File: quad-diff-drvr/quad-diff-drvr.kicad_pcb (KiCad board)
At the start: 2 copper layers, 65 x 56 mm, 58 parts, among them J1 Raspberry_Pi_2_3, J2 Conn_01x04, J3 Conn_01x04, J4 Conn_01x04, J5 Conn_01x04, J6 Conn_01x04, U1 INA3221, U2 74LS153, U3 74LS153, U4 74LS153, U5 PCA9555PW, U6 LTC1688, U7 SLG5NT1581V, U8 SLG5NT1581V

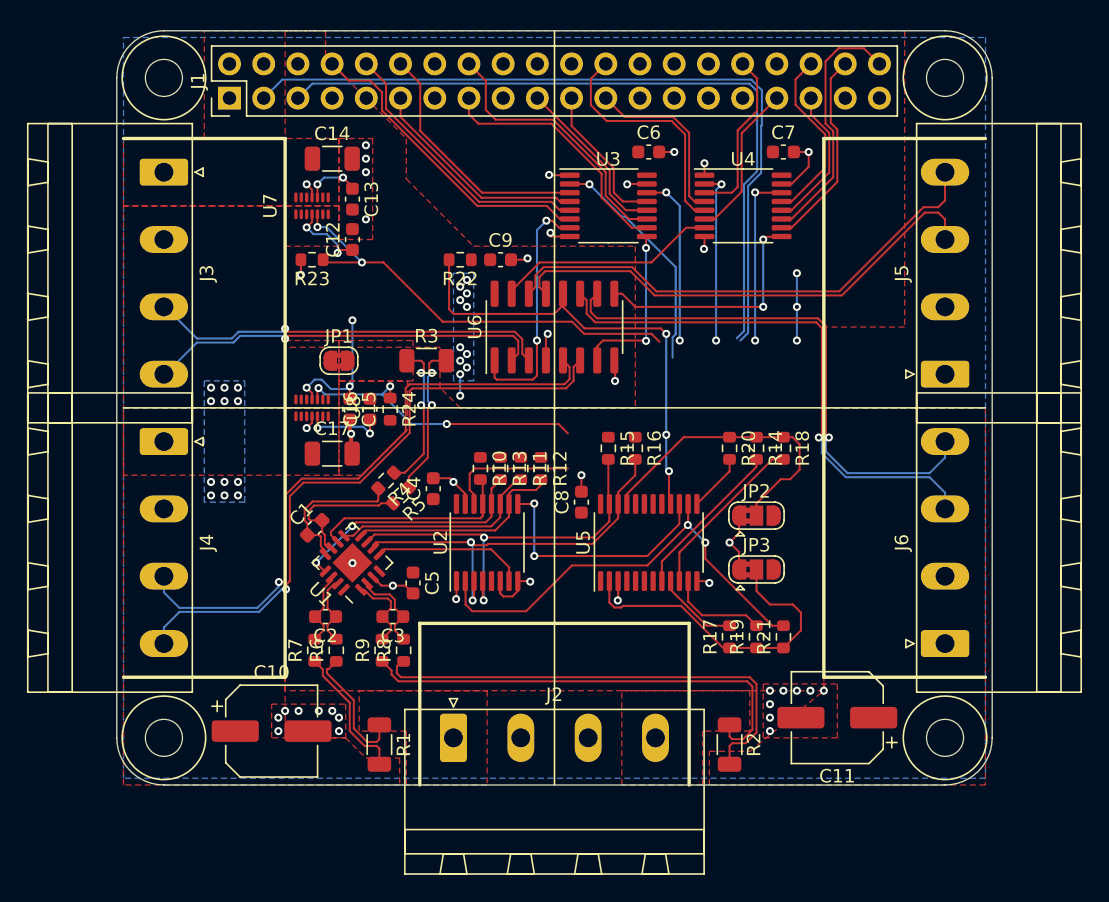
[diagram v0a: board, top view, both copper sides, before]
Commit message: qdd: VB high side switches
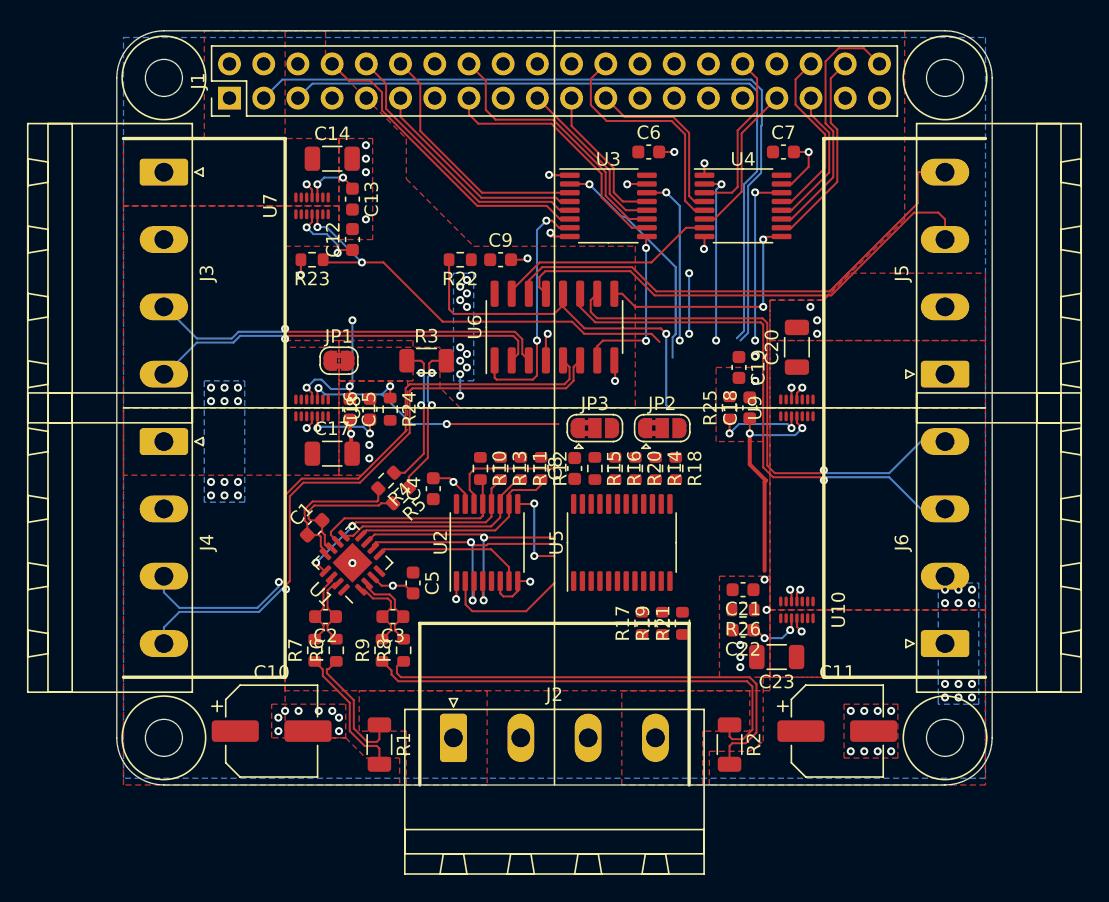
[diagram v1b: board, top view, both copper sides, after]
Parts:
- added C18: 100nF, Capacitor_SMD:C_0603_1608Metric, F.Cu at (114.5, 100.0)
- added C19: 4.7nF, Capacitor_SMD:C_0603_1608Metric, F.Cu at (113.7, 97.0)
- added C20: 10uF, Capacitor_SMD:C_1206_3216Metric, F.Cu at (118.0, 95.5)
- added C21: 100nF, Capacitor_SMD:C_0603_1608Metric, F.Cu at (114.0, 113.5)
- added C22: 4.7nF, Capacitor_SMD:C_0603_1608Metric, F.Cu at (114.0, 116.5)
- added C23: 10uF, Capacitor_SMD:C_1206_3216Metric, F.Cu at (116.5, 118.5)
- added R25: 10k, Resistor_SMD:R_0603_1608Metric, F.Cu at (113.0, 100.0)
- added R26: 10k, Resistor_SMD:R_0603_1608Metric, F.Cu at (114.0, 115.0)
- added U10: SLG5NT1581V, octo-pcb:QFN-28_1x3_Pitch0.4mm, F.Cu at (118.0, 115.0)
- added U9: SLG5NT1581V, octo-pcb:QFN-28_1x3_Pitch0.4mm, F.Cu at (118.0, 100.0)
- moved JP3 15.9 mm to (103.0, 101.5)
- moved JP2 9.55 mm to (108.0, 101.5)
- moved R18 8.14 mm to (109.0, 104.5)
- moved R14 7.65 mm to (107.5, 104.5)
- moved R21 7.57 mm to (109.5, 116.0)
- moved R20 7.16 mm to (106.0, 104.5)
- moved R19 7.07 mm to (108.0, 116.0)
- moved R17 6.58 mm to (106.5, 116.0)
- moved C8 2.55 mm to (101.5, 104.5)
- moved R16 2.12 mm to (104.5, 104.5)
- moved U5 2.00 mm to (105.0, 110.0)
- moved R15 1.80 mm to (103.0, 104.5)
- moved C11 1.00 mm to (121.0, 124.0), turned to 0 degrees
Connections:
- J5 pad 1: /VB -> /VB2
- J6 pad 1: /VB -> /VB3
- U5 pad 6: (no net) -> /VEN2
- U5 pad 7: (no net) -> /VEN3
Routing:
- net /A1: track 24.3 -> 0.00 mm
- net /PM_A1: track 33.6 -> 9.42 mm, vias 2 -> 0
- net /A0: track 22.6 -> 0.00 mm
- net +5V: track 29.8 -> 47.9 mm, vias 18 -> 21
- net /M1_A0: track 25.7 -> 13.0 mm
- net /M0_A0: track 24.8 -> 12.9 mm
- net /PM_STAT: track 18.4 -> 6.64 mm
- net /SCL: track 83.9 -> 73.6 mm
- net /SDA: track 86.7 -> 77.5 mm
- net /M1_A1: track 20.4 -> 13.0 mm
- net /DEN: track 35.6 -> 28.4 mm, vias 3 -> 1
- net /VEN2: track 0.00 -> 6.96 mm, vias 0 -> 2
- net /M0_A1: track 23.4 -> 17.2 mm
- net GND: track 44.1 -> 38.0 mm, vias 43 -> 63
- net /PM_A0: track 14.2 -> 8.84 mm
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- added copper zone on B.Cu, net /VB
- added copper zone on F.Cu, net /VB2
- added copper zone on F.Cu, net /VB3

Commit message: qdd: quick and dirty route done
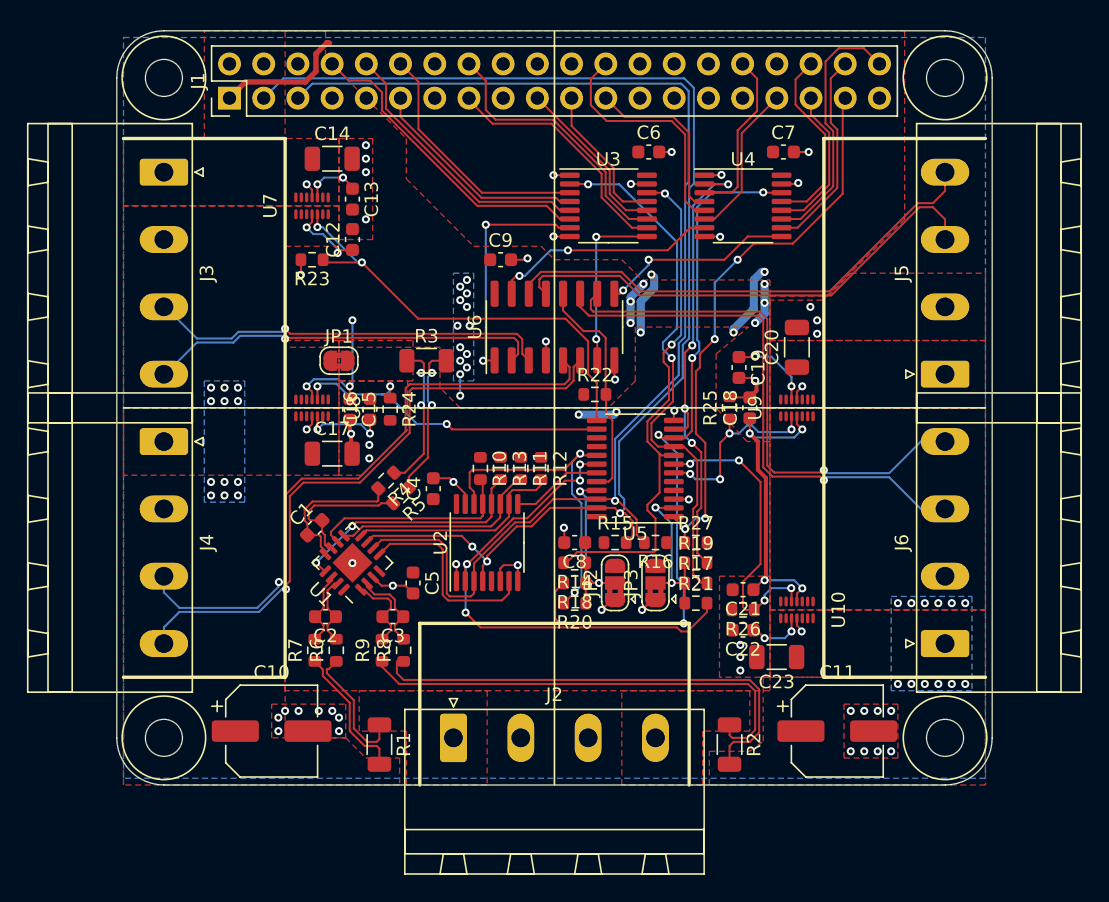
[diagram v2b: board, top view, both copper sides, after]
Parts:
- added R27: 10k, Resistor_SMD:R_0603_1608Metric, F.Cu at (110.5, 110.0)
- moved R22 14.1 mm to (103.0, 99.0), turned to 0 degrees
- moved JP3 12.3 mm to (107.5, 113.0), turned to 90 degrees
- moved JP2 12.0 mm to (104.5, 113.0), turned to 90 degrees
- moved R18 11.3 mm to (101.5, 113.0), turned to 180 degrees
- moved R20 11.0 mm to (101.5, 114.5), turned to 180 degrees
- moved R14 9.22 mm to (101.5, 111.5), turned to 180 degrees
- moved R16 6.26 mm to (107.5, 110.0), turned to 180 degrees
- moved R15 5.70 mm to (104.5, 110.0), turned to 0 degrees
- moved U5 5.59 mm to (106.0, 104.5), turned to 180 degrees
- moved C8 5.50 mm to (101.5, 110.0), turned to 180 degrees
- moved R19 5.15 mm to (110.5, 111.5), turned to 0 degrees
- moved R17 5.00 mm to (110.5, 113.0), turned to 0 degrees
- moved R21 1.80 mm to (110.5, 114.5), turned to 0 degrees
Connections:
- J1 pad 37: (no net) -> /INTn
- U5 pad 1: (no net) -> /INTn
- U5 pad 13: /PM_A0 -> /VEN0
- U5 pad 14: /PM_A1 -> /VEN1
- U5 pad 15: /PM_STAT -> (no net)
- U5 pad 16: /DEN -> (no net)
- U5 pad 17: (no net) -> /PM_A0
- U5 pad 18: (no net) -> /PM_A1
- U5 pad 19: (no net) -> /PM_STAT
- U5 pad 20: (no net) -> /DEN
- U5 pad 4: /VEN0 -> (no net)
- U5 pad 5: /VEN1 -> (no net)
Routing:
- net /INTn: track 0.00 -> 41.9 mm, vias 0 -> 4
- net /M1_A0: track 13.0 -> 53.8 mm, vias 2 -> 4
- net /PM_A1: track 9.42 -> 38.1 mm, vias 0 -> 4
- net /M0_A0: track 12.9 -> 39.2 mm
- net /M0_A1: track 17.2 -> 39.8 mm, vias 1 -> 2
- net /M1_A1: track 13.0 -> 35.3 mm, vias 2 -> 4
- net /VEN3: track 0.92 -> 22.6 mm, vias 3 -> 4
- net /SCL: track 73.6 -> 92.8 mm, vias 2 -> 1
- net +3V3: track 4.50 -> 23.1 mm, vias 2 -> 6
- net /SDA: track 77.5 -> 94.1 mm, vias 2 -> 3
- net /PM_A0: track 8.84 -> 24.7 mm, vias 0 -> 2
- net /A0: track 0.00 -> 14.1 mm, vias 0 -> 2
- net /A1: track 0.00 -> 13.0 mm, vias 0 -> 2
- net +5V: track 47.9 -> 59.3 mm, vias 21 -> 30
- net /DEN: track 28.4 -> 17.3 mm, vias 1 -> 0
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
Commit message: qdd: cleaned up silkscreen
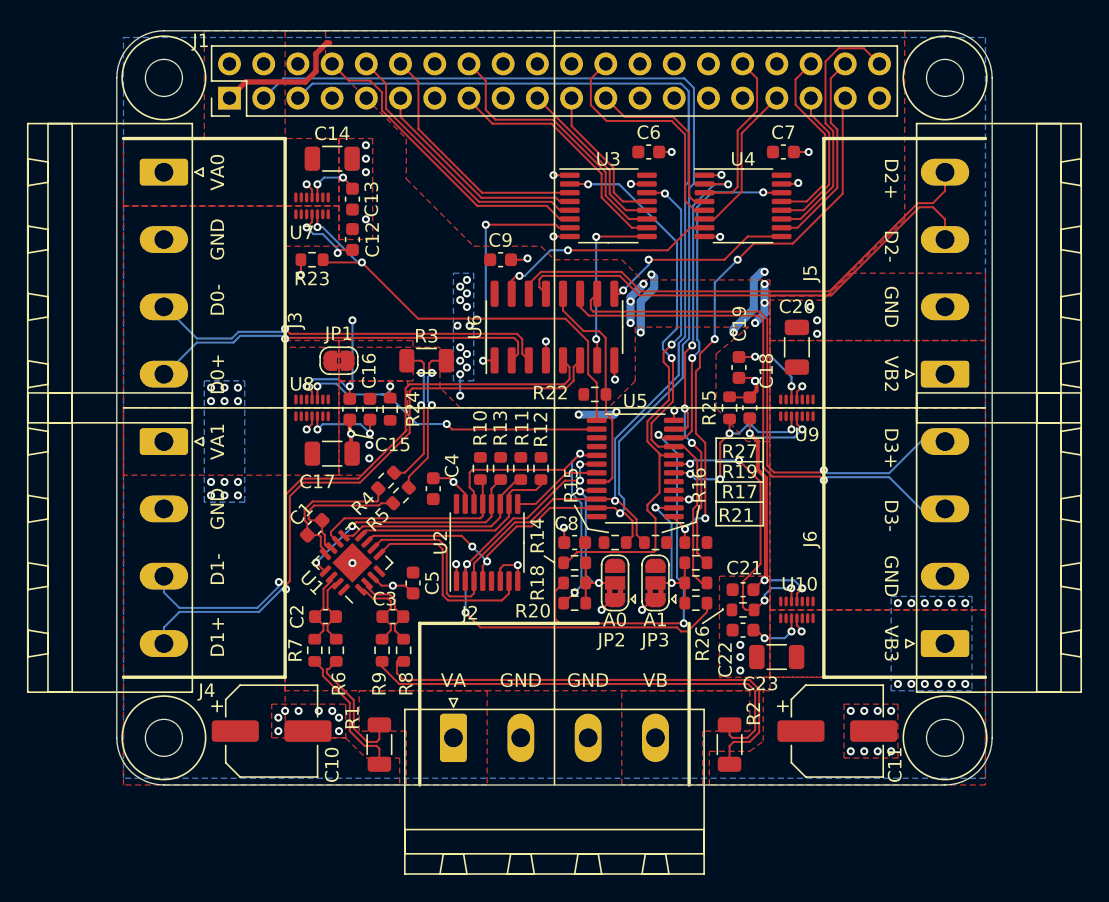
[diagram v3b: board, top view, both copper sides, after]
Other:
- board text added: "A0"
- board text added: "A1"
- board text added: "D0+"
- board text added: "D0-"
- board text added: "D1+"
- board text added: "D1-"
- board text added: "D2+"
- board text added: "D2-"
- board text added: "D3+"
- board text added: "D3-"
- board text added: "GND"
- board text added: "VA"
- board text added: "VA0"
- board text added: "VA1"
- board text added: "VB"
- board text added: "VB2"
- board text added: "VB3"
